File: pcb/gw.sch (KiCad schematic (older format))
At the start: 19 parts, among them IC1 ATMEGA8A-P, P1 CONN_CLUNET, P2 USB_OTG, Q1 BC849, U1 FT232RL, Y1 Crystal

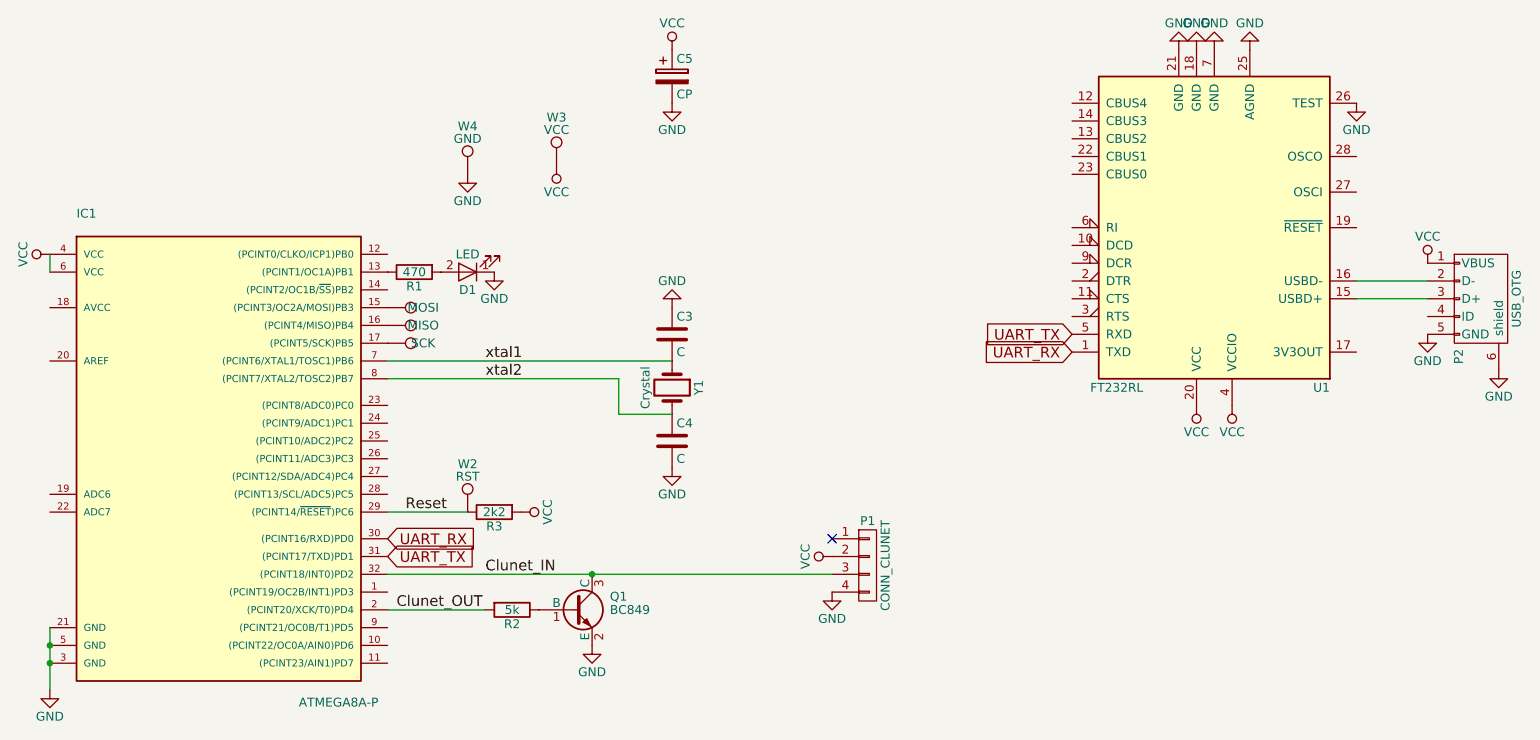
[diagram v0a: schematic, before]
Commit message: Switch PCB sides, TQFP32 atmega
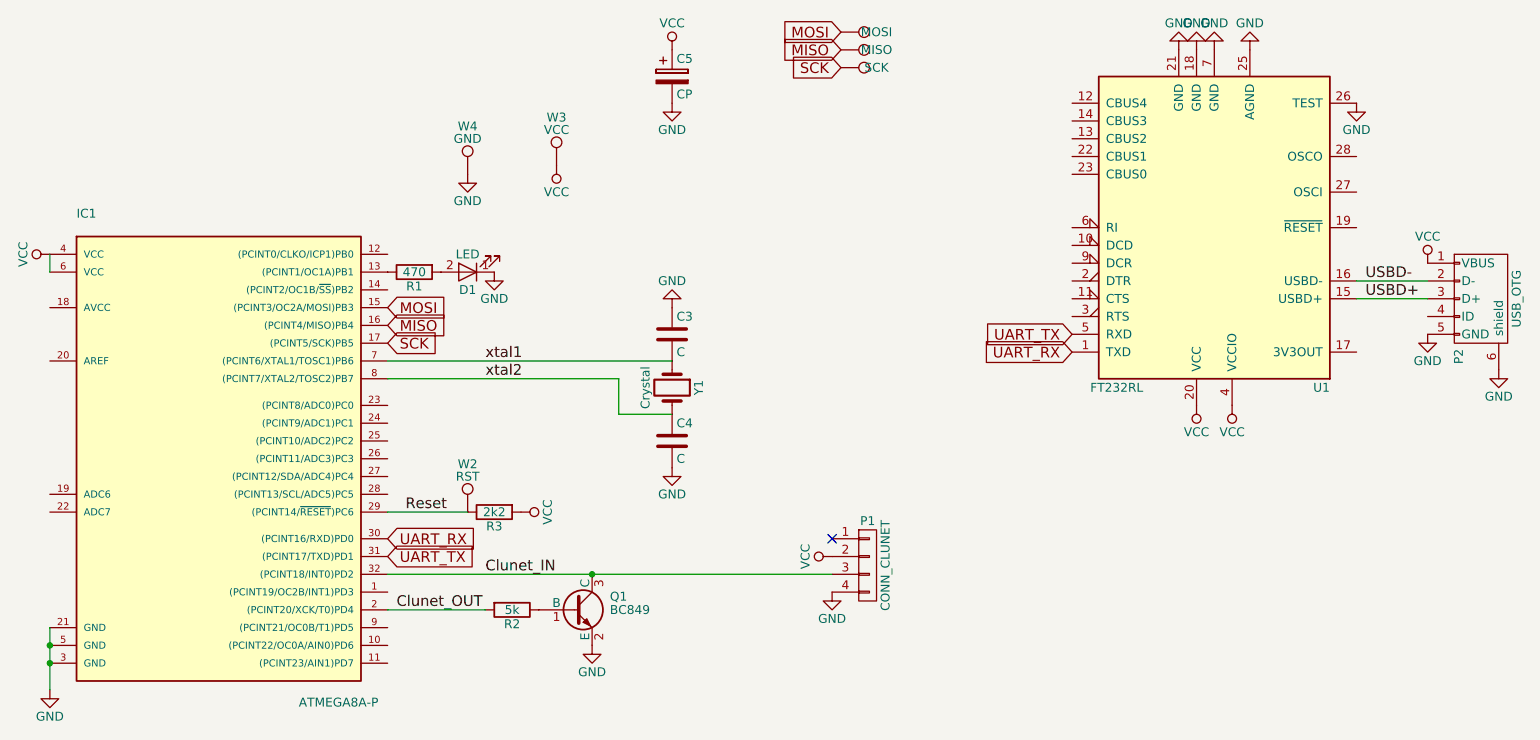
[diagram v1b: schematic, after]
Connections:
- net MOSI: now reaches IC1.15 ((PCINT3/OC2A/MOSI)PB3), W1.1
- net MISO: now reaches IC1.16 ((PCINT4/MISO)PB4), W5.1
- net SCK: now reaches IC1.17 ((PCINT5/SCK)PB5), W6.1
- net USBD+: now reaches P2.3 (D+), U1.15 (USBD+)
- net USBD-: now reaches P2.2 (D-), U1.16 (USBD-)
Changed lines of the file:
@@
 UART_RX
-$Comp
-L TEST_1P W1
-U 1 1 5A591DD5
-P 3900 2450
-F 0 "W1" H 3900 2720 50  0001 C CNN
-F 1 "MOSI" V 3900 2650 50  0000 C CNN
-F 2 "Measurement_Points:Measurement_Point_Round-SMD-Pad_Small" H 4100 2450 50  0001 C CNN
-F 3 "" H 4100 2450 50  0000 C CNN
-	1    3900 2450
-	0    1    1    0
-$EndComp
 $Comp
 L TEST_1P W5
 U 1 1 5A591D37
-P 3900 2550
-F 0 "W5" H 3900 2820 50  0001 C CNN
-F 1 "MISO" V 3900 2750 50  0000 C CNN
-F 2 "Measurement_Points:Measurement_Point_Round-SMD-Pad_Small" H 4100 2550 50  0001 C CNN
-F 3 "" H 4100 2550 50  0000 C CNN
-	1    3900 2550
+P 6450 1000
+F 0 "W5" H 6450 1270 50  0001 C CNN
+F 1 "MISO" V 6450 1200 50  0000 C CNN
+F 2 "Measurement_Points:Measurement_Point_Round-SMD-Pad_Small" H 6650 1000 50  0001 C CNN
+F 3 "" H 6650 1000 50  0000 C CNN
+	1    6450 1000
 	0    1    1    0
 $EndComp
@@
 L TEST_1P W6
 U 1 1 5A591E2D
-P 3900 2650
-F 0 "W6" H 3900 2920 50  0001 C CNN
-F 1 "SCK" V 3900 2850 50  0000 C CNN
-F 2 "Measurement_Points:Measurement_Point_Round-SMD-Pad_Small" H 4100 2650 50  0001 C CNN
-F 3 "" H 4100 2650 50  0000 C CNN
-	1    3900 2650
+P 6450 1100
+F 0 "W6" H 6450 1370 50  0001 C CNN
+F 1 "SCK" V 6450 1300 50  0000 C CNN
+F 2 "Measurement_Points:Measurement_Point_Round-SMD-Pad_Small" H 6650 1100 50  0001 C CNN
+F 3 "" H 6650 1100 50  0000 C CNN
+	1    6450 1100
 	0    1    1    0
 $EndComp
@@
 Text Label 4450 2850 0    60   ~ 0
 xtal2
+Text Label 9400 2300 0    60   ~ 0
+USBD-
+Text Label 9400 2400 0    60   ~ 0
+USBD+
+Text GLabel 3900 2450 2    60   Input ~ 0
+MOSI
+$Comp
+L TEST_1P W1
+U 1 1 5A591DD5
+P 6450 900
+F 0 "W1" H 6450 1170 50  0001 C CNN
+F 1 "MOSI" V 6450 1100 50  0000 C CNN
+F 2 "Measurement_Points:Measurement_Point_Round-SMD-Pad_Small" H 6650 900 50  0001 C CNN
+F 3 "" H 6650 900 50  0000 C CNN
+	1    6450 900
+	0    1    1    0
+$EndComp
+Text GLabel 3900 2550 2    60   Input ~ 0
+MISO
+Text GLabel 3900 2650 2    60   Input ~ 0
+SCK
+Text GLabel 6450 900  0    60   Input ~ 0
+MOSI
+Text GLabel 6450 1000 0    60   Input ~ 0
+MISO
+Text GLabel 6450 1100 0    60   Input ~ 0
+SCK
 $EndSCHEMATC
